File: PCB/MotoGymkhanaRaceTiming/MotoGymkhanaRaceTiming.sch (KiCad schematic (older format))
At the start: 27 parts, among them U1 LM2577T-ADJ_NOPB, U2 PC817, U3 PC817

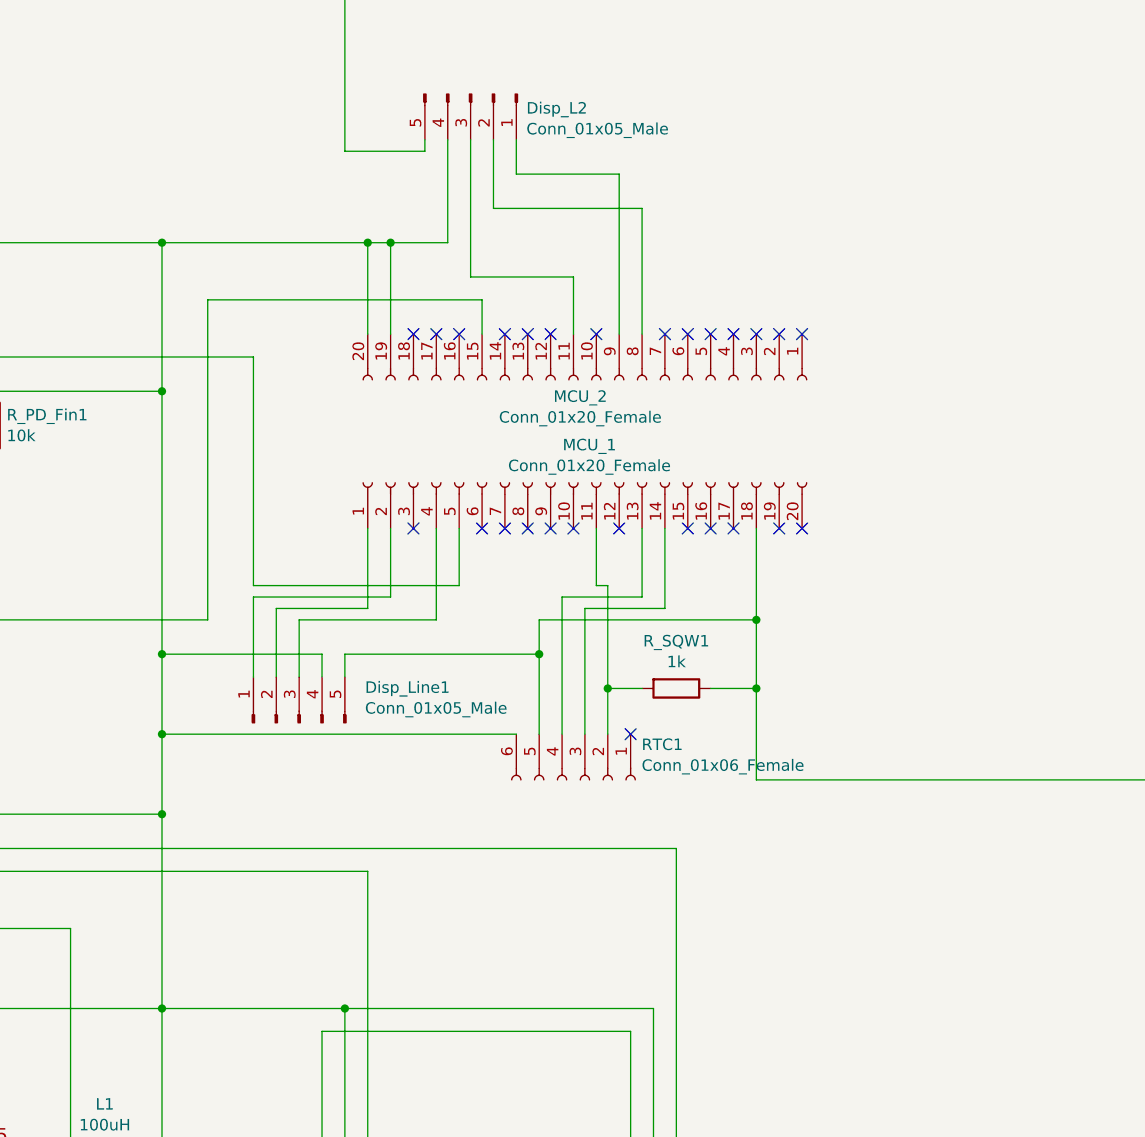
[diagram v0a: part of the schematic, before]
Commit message: Better PCB, now with jumpers (or headers to wire switches to) for configuration
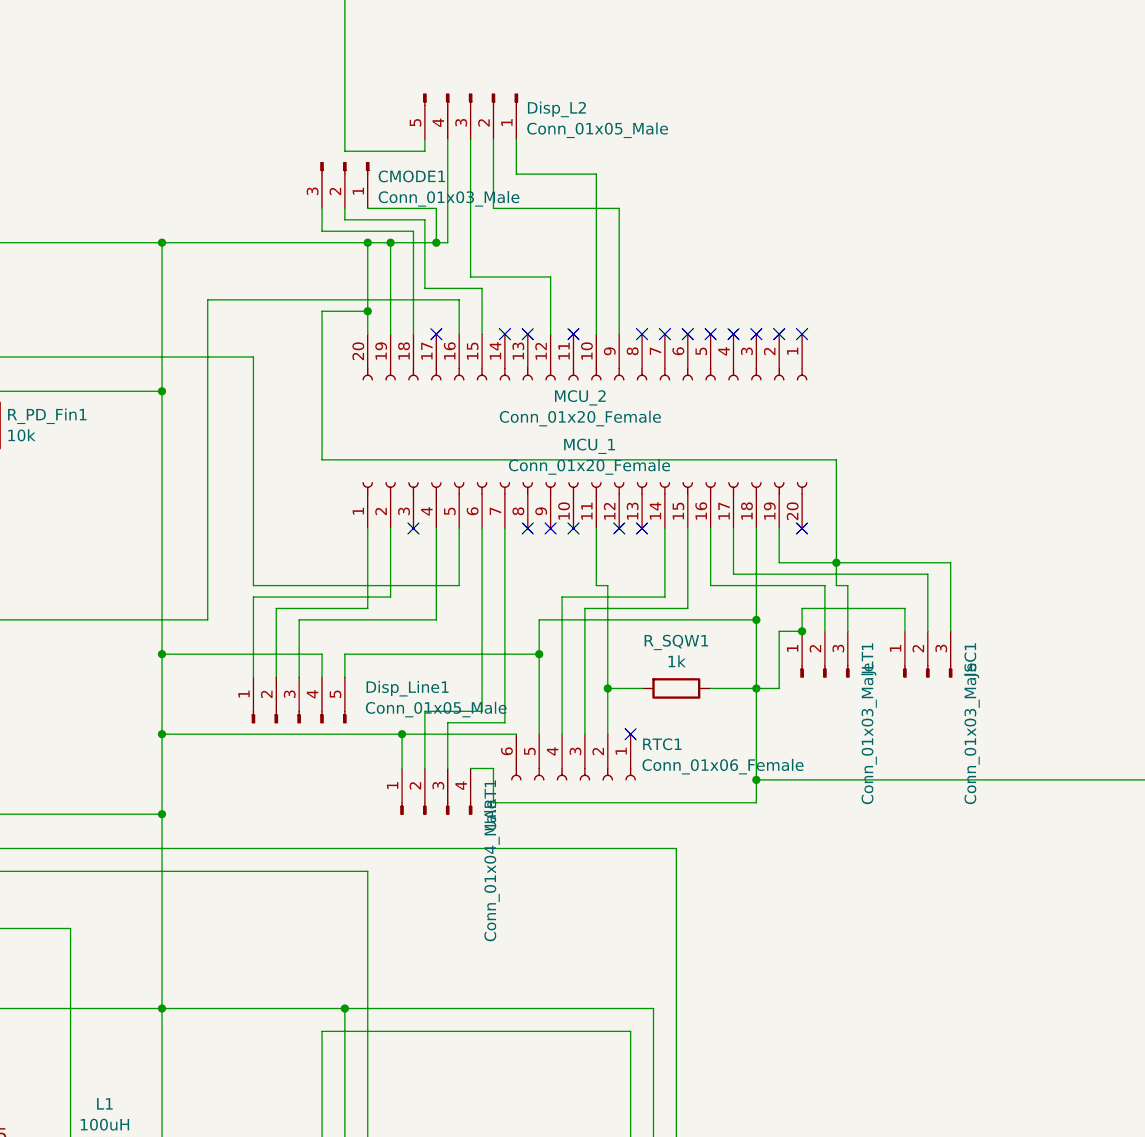
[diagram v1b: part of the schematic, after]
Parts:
- added CMODE1, JLT1, JSC1: Conn_01x03_Male, Connector_PinHeader_2.54mm:PinHeader_1x03_P2.54mm_Vertical, symbol Connector:Conn_01x03_Male
- added UART1: Conn_01x04_Male, Connector_PinHeader_2.54mm:PinHeader_1x04_P2.54mm_Vertical, symbol Connector:Conn_01x04_Male
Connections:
- net at MCU_2.10 (Pin_10): now also Disp_L2.1 (Pin_1)
- net at MCU_2.11 (Pin_11): no longer Disp_L2.3 (Pin_3)
- net at MCU_2.12 (Pin_12): now also Disp_L2.3 (Pin_3)
- net at LED_FIN1.2 (A), R_PD_Fin1.2, U3.3: now also MCU_2.16 (Pin_16); no longer MCU_2.15 (Pin_15)
- net at MCU_2.18 (Pin_18): now also CMODE1.3 (Pin_3)
- net at C1.2, C2.1, C3.2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: now also MCU_1.19 (Pin_19), CMODE1.1 (Pin_1), JLT1.3 (Pin_3), JSC1.3 (Pin_3), UART1.1 (Pin_1)
- net at MCU_2.8 (Pin_8): no longer Disp_L2.2 (Pin_2)
- net at MCU_2.9 (Pin_9): now also Disp_L2.2 (Pin_2); no longer Disp_L2.1 (Pin_1)
- net at MCU_1.13 (Pin_13): no longer RTC1.4 (Pin_4)
- net at MCU_1.14 (Pin_14): now also RTC1.4 (Pin_4); no longer RTC1.3 (Pin_3)
- net at MCU_1.15 (Pin_15): now also RTC1.3 (Pin_3)
- net at MCU_1.16 (Pin_16): now also JLT1.2 (Pin_2)
- net at MCU_1.17 (Pin_17): now also JSC1.2 (Pin_2)
- net at C1.1, C3.1, Disp_L2.5 (Pin_5)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: now also JLT1.1 (Pin_1), JSC1.1 (Pin_1), UART1.4 (Pin_4)
- net at MCU_1.6 (Pin_6): now also UART1.2 (Pin_2)
- net at MCU_1.7 (Pin_7): now also UART1.3 (Pin_3)
- new net: CMODE1.2 (Pin_2), MCU_2.15 (Pin_15)
- no-connect marks 30 -> 23
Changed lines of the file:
@@
 	1250 2750 3600 2750
 Wire Wire Line
-	4500 2750 4500 3150
+	4500 2750 4500 3050
 Wire Wire Line
 	4500 2750 4600 2750
@@
 Wire Wire Line
 	3800 4400 3800 3000
-Wire Wire Line
-	3800 3000 5000 3000
-Wire Wire Line
-	5000 3000 5000 3150
 Connection ~ 2850 4400
 Wire Wire Line
@@
 $EndComp
 Wire Wire Line
-	5150 4900 3600 4900
+	5150 4900 4650 4900
 Connection ~ 3600 4900
 Wire Wire Line
@@
 	5450 4900 5450 4350
 Wire Wire Line
-	5800 4350 5800 4000
-Wire Wire Line
-	5450 4350 5800 4350
-Wire Wire Line
 	5350 4900 5350 4300
-Wire Wire Line
-	5350 4300 5700 4300
-Wire Wire Line
-	5700 4300 5700 4000
 $Comp
 L Connector:Conn_01x05_Male Disp_L2
@@
 	4850 2300 4850 2750
 Wire Wire Line
-	4850 2750 4600 2750
+	4850 2750 4800 2750
 Connection ~ 4600 2750
 Wire Wire Line
 	4950 2300 4950 2900
 Wire Wire Line
-	4950 2900 5400 2900
-Wire Wire Line
-	5400 2900 5400 3150
-Wire Wire Line
-	5600 3150 5600 2450
-Wire Wire Line
-	5600 2450 5150 2450
-Wire Wire Line
 	5150 2450 5150 2300
 Wire Wire Line
 	5050 2300 5050 2600
-Wire Wire Line
-	5050 2600 5700 2600
-Wire Wire Line
-	5700 2600 5700 3150
 Wire Wire Line
 	4400 4650 4400 4550
@@
 NoConn ~ 5900 3150
 NoConn ~ 5800 3150
-NoConn ~ 5500 3150
-NoConn ~ 5300 3150
 NoConn ~ 5200 3150
 NoConn ~ 5100 3150
-NoConn ~ 4900 3150
 NoConn ~ 4800 3150
-NoConn ~ 4700 3150
 NoConn ~ 6400 4000
-NoConn ~ 6300 4000
-NoConn ~ 6100 4000
-NoConn ~ 6000 4000
-NoConn ~ 5900 4000
 NoConn ~ 5600 4000
 NoConn ~ 5400 4000
 NoConn ~ 5300 4000
 NoConn ~ 5200 4000
-NoConn ~ 5100 4000
-NoConn ~ 5000 4000
 NoConn ~ 4700 4000
 NoConn ~ 5650 4900
@@
 	1150 2050 1250 2050
 Connection ~ 1150 1950
+Wire Wire Line
+	5450 4350 5900 4350
+Wire Wire Line
+	5900 4350 5900 4000
+Wire Wire Line
+	5800 4300 5800 4000
+Wire Wire Line
+	5350 4300 5800 4300
+NoConn ~ 5700 4000
+Wire Wire Line
+	4500 3050 4300 3050
+Wire Wire Line
+	4300 3050 4300 3700
+Wire Wire Line
+	4300 3700 6550 3700
+Wire Wire Line
+	6550 3700 6550 4150
+Wire Wire Line
+	6550 4150 6300 4150
+Wire Wire Line
+	6300 4150 6300 4000
+Connection ~ 4500 3050
+Wire Wire Line
+	4500 3050 4500 3150
+$Comp
+L Connector:Conn_01x03_Male JLT1
+U 1 1 5ED22EE5
+P 6500 4650
+F 0 "JLT1" H 6654 4462 50  0000 R CNN
+F 1 "Conn_01x03_Male" H 6563 4462 50  0000 R CNN
+F 2 "Connector_PinHeader_2.54mm:PinHeader_1x03_P2.54mm_Vertical" H 6500 4650 50  0001 C CNN
+F 3 "~" H 6500 4650 50  0001 C CNN
+	1    6500 4650
+	0    -1   -1   0
+$EndComp
+$Comp
+L Connector:Conn_01x03_Male JSC1
+U 1 1 5ED24AEC
+P 6950 4650
+F 0 "JSC1" H 7104 4462 50  0000 R CNN
+F 1 "Conn_01x03_Male" H 7013 4462 50  0000 R CNN
+F 2 "Connector_PinHeader_2.54mm:PinHeader_1x03_P2.54mm_Vertical" H 6950 4650 50  0001 C CNN
+F 3 "~" H 6950 4650 50  0001 C CNN
+	1    6950 4650
+	0    -1   -1   0
+$EndComp
+Wire Wire Line
+	6500 4450 6500 4250
+Wire Wire Line
+	6500 4250 6000 4250
+Wire Wire Line
+	6000 4250 6000 4000
+Wire Wire Line
+	6950 4450 6950 4200
+Wire Wire Line
+	6950 4200 6100 4200
+Wire Wire Line
+	6100 4200 6100 4000
+Wire Wire Line
+	6200 4700 6300 4700
+Wire Wire Line
+	6300 4700 6300 4450
+Wire Wire Line
+	6300 4450 6400 4450
+Wire Wire Line
+	6400 4450 6400 4350
+Wire Wire Line
+	6400 4350 6850 4350
+Wire Wire Line
+	6850 4350 6850 4450
+Connection ~ 6400 4450
+Wire Wire Line
+	6550 4150 7050 4150
+Wire Wire Line
+	7050 4150 7050 4450
+Connection ~ 6550 4150
+Wire Wire Line
+	5050 2600 5600 2600
+Wire Wire Line
+	5600 2600 5600 3150
+Wire Wire Line
+	5150 2450 5500 2450
+Wire Wire Line
+	5500 2450 5500 3150
+NoConn ~ 5700 3150
+Wire Wire Line
+	6600 4450 6600 4250
+Wire Wire Line
+	6600 4250 6550 4250
+Wire Wire Line
+	6550 4250 6550 4150
+Wire Wire Line
+	4950 2900 5300 2900
+Wire Wire Line
+	5300 2900 5300 3150
+NoConn ~ 5400 3150
+$Comp
+L Connector:Conn_01x04_Male UART1
+U 1 1 5EDA4F4A
+P 4750 5250
+F 0 "UART1" H 4904 4962 50  0000 R CNN
+F 1 "Conn_01x04_Male" H 4813 4962 50  0000 R CNN
+F 2 "Connector_PinHeader_2.54mm:PinHeader_1x04_P2.54mm_Vertical" H 4750 5250 50  0001 C CNN
+F 3 "~" H 4750 5250 50  0001 C CNN
+	1    4750 5250
+	0    -1   -1   0
+$EndComp
+Wire Wire Line
+	5000 4000 5000 4800
+Wire Wire Line
+	4750 4800 4750 5050
+Wire Wire Line
+	5000 4800 4750 4800
+Wire Wire Line
+	4850 5050 4850 4850
+Wire Wire Line
+	4850 4850 5100 4850
+Wire Wire Line
+	5100 4850 5100 4000
+Wire Wire Line
+	4650 4900 4650 5050
+Connection ~ 4650 4900
+Wire Wire Line
+	4650 4900 3600 4900
+Wire Wire Line
+	4950 5050 5050 5050
+Wire Wire Line
+	5050 5050 5050 5200
+Wire Wire Line
+	5050 5200 6200 5200
+Wire Wire Line
+	6200 5200 6200 5100
+Connection ~ 6200 5100
+Wire Wire Line
+	3800 3000 4900 3000
+Wire Wire Line
+	4900 3000 4900 3150
+$Comp
+L Connector:Conn_01x03_Male CMODE1
+U 1 1 5EE0E5C1
+P 4400 2400
+F 0 "CMODE1" V 4462 2544 50  0000 L CNN
+F 1 "Conn_01x03_Male" V 4553 2544 50  0000 L CNN
+F 2 "Connector_PinHeader_2.54mm:PinHeader_1x03_P2.54mm_Vertical" H 4400 2400 50  0001 C CNN
+F 3 "~" H 4400 2400 50  0001 C CNN
+	1    4400 2400
+	0    1    1    0
+$EndComp
+Wire Wire Line
+	4300 2600 4300 2700
+Wire Wire Line
+	4300 2700 4700 2700
+Wire Wire Line
+	4400 2600 4400 2650
+Wire Wire Line
+	4400 2650 4750 2650
+Wire Wire Line
+	4750 2650 4750 2950
+Wire Wire Line
+	4750 2950 5000 2950
+Wire Wire Line
+	5000 2950 5000 3150
+Wire Wire Line
+	4500 2600 4800 2600
+Wire Wire Line
+	4800 2600 4800 2750
+Connection ~ 4800 2750
+Wire Wire Line
+	4600 2750 4800 2750
+Wire Wire Line
+	4700 2700 4700 3150
 $EndSCHEMATC

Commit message: PCB update
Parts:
- added Btn1, Btn2: Conn_01x02_Male, Connector_PinHeader_2.54mm:PinHeader_1x02_P2.54mm_Vertical, symbol Connector:Conn_01x02_Male
- added H1, H2, H3, H4: MountingHole_Pad, MountingHole:MountingHole_3.2mm_M3_Pad_Via, symbol Mechanical:MountingHole_Pad
- added R33: 33k, Resistor_THT:R_Axial_DIN0207_L6.3mm_D2.5mm_P10.16mm_Horizontal, symbol Device:R
- added R39: 3k9, Resistor_THT:R_Axial_DIN0207_L6.3mm_D2.5mm_P10.16mm_Horizontal, symbol Device:R
- added R_PD_B1, R_PD_B2: 10k, Resistor_THT:R_Axial_DIN0207_L6.3mm_D2.5mm_P10.16mm_Horizontal, symbol Device:R
- C1: footprint Capacitor_THT:CP_Radial_D13.0mm_P5.00mm -> Capacitor_THT:CP_Radial_D8.0mm_P5.00mm
- C2, C3: footprint Capacitor_THT:C_Radial_D10.0mm_H12.5mm_P5.00mm -> Capacitor_THT:C_Disc_D4.7mm_W2.5mm_P5.00mm
- C4: footprint Capacitor_THT:CP_Radial_D13.0mm_P5.00mm -> Capacitor_THT:CP_Radial_D10.0mm_P5.00mm
- Disp_L2, Disp_Line1: footprint Connector_PinHeader_2.54mm:PinHeader_1x05_P2.54mm_Horizontal -> MotoGymkhanaRaceTiming:DisplayLineConnector
- L1: footprint Inductor_THT:L_Toroid_Vertical_L10.0mm_W5.0mm_P5.08mm -> Inductor_THT:L_Radial_D7.0mm_P3.00mm
- SENS_FIN1, SENS_START1: footprint TerminalBlock:TerminalBlock_Altech_AK300-3_P5.00mm -> MotoGymkhanaRaceTiming:SensorConnector
- U1: symbol 2020-05-24_13-28-23:LM2577T-ADJ_NOPB -> MotoGymkhanaRaceTiming-rescue:LM2577T-ADJ_NOPB-2020-05-24_13-28-23
- UART1: footprint Connector_PinHeader_2.54mm:PinHeader_1x04_P2.54mm_Vertical -> MotoGymkhanaRaceTiming:UART
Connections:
- net at CMODE1.3 (Pin_3), MCU_2.18 (Pin_18): now also Btn1.1 (Pin_1), Btn2.1 (Pin_1)
- net at C1.2, C2.1, C3.2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: now also H1.1, H2.1, H3.1, H4.1, R39.1, R_PD_B1.2, R_PD_B2.2
- net at MCU_2.5 (Pin_5): now also Btn2.2 (Pin_2), R_PD_B2.1
- net at MCU_2.6 (Pin_6): now also Btn1.2 (Pin_2), R_PD_B1.1
- net at MCU_1.14 (Pin_14): now also RTC1.3 (Pin_3); no longer RTC1.4 (Pin_4)
- net at MCU_1.15 (Pin_15): now also RTC1.4 (Pin_4); no longer RTC1.3 (Pin_3)
- net at C4.1, D1.1 (K), SENS_FIN1.3 (Pin_3)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: now also R33.2; no longer U1.2 (FB)
- new net: R33.1, R39.2, U1.2 (FB)
- no-connect marks 23 -> 21

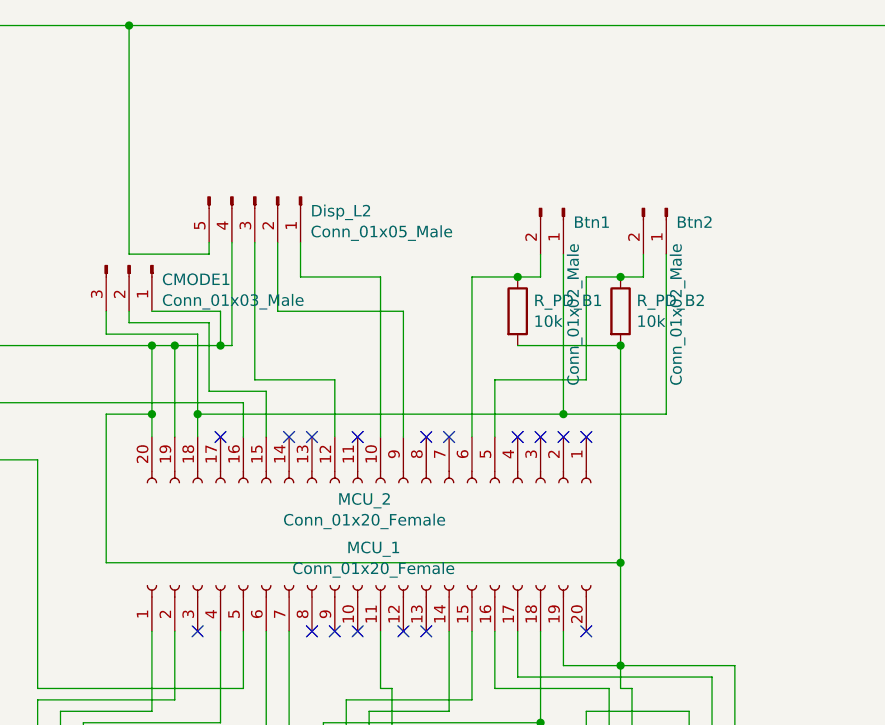
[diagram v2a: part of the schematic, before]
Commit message: Update for issue #9
- Adding text to RTC socket
- Adding UART2
- Trace width for 5V net updated
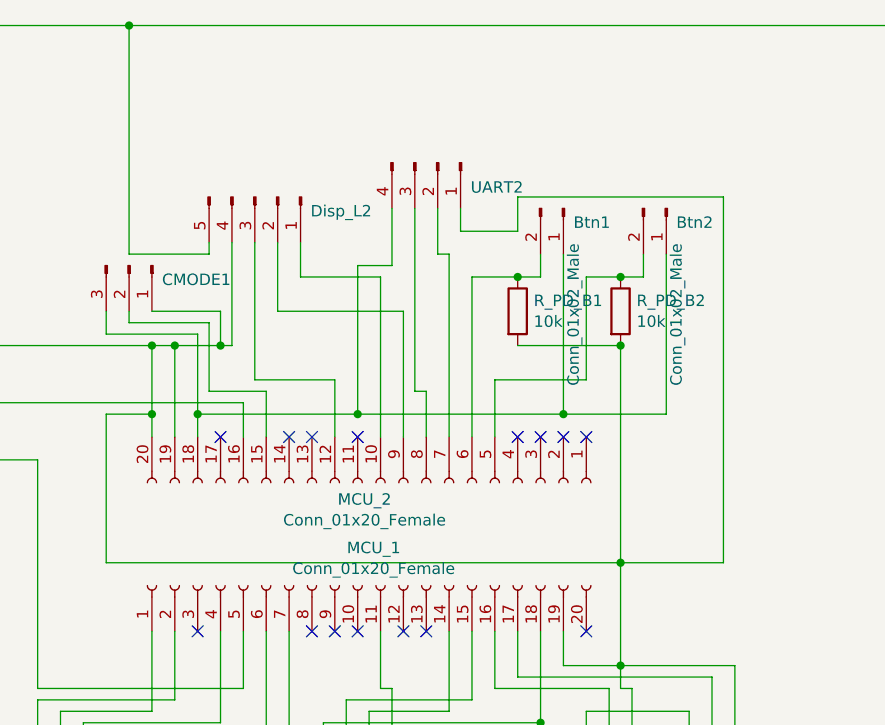
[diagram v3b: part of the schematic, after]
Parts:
- added UART2: Conn_01x04_Male, MotoGymkhanaRaceTiming:UART, symbol Connector:Conn_01x04_Male
- RTC1: footprint Connector_PinSocket_2.54mm:PinSocket_1x06_P2.54mm_Vertical -> MotoGymkhanaRaceTiming:RTC_Socket
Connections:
- net at Btn1.1 (Pin_1), Btn2.1 (Pin_1), CMODE1.3 (Pin_3)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: now also UART2.4 (Pin_4)
- net at C1.2, C2.1, C3.2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: now also UART2.1 (Pin_1)
- net at MCU_2.7 (Pin_7): now also UART2.2 (Pin_2)
- net at MCU_2.8 (Pin_8): now also UART2.3 (Pin_3)
- no-connect marks 21 -> 19
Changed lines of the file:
@@
 F 0 "RTC1" V 5296 5348 50  0000 L CNN
 F 1 "Conn_01x06_Female" V 5387 5348 50  0001 L CNN
-F 2 "Connector_PinSocket_2.54mm:PinSocket_1x06_P2.54mm_Vertical" H 5450 5100 50  0001 C CNN
+F 2 "MotoGymkhanaRaceTiming:RTC_Socket" H 5450 5100 50  0001 C CNN
 F 3 "~" H 5450 5100 50  0001 C CNN
 	1    5450 5100
@@
 P 4950 2100
 F 0 "Disp_L2" V 5012 2344 50  0000 L CNN
-F 1 "Conn_01x05_Male" V 5103 2344 50  0000 L CNN
+F 1 "Conn_01x05_Male" V 5103 2344 50  0001 L CNN
 F 2 "MotoGymkhanaRaceTiming:DisplayLineConnector" H 4950 2100 50  0001 C CNN
 F 3 "~" H 4950 2100 50  0001 C CNN
@@
 NoConn ~ 6200 3150
 NoConn ~ 6100 3150
-NoConn ~ 5800 3150
 NoConn ~ 5200 3150
 NoConn ~ 5100 3150
@@
 Wire Wire Line
 	5500 2450 5500 3150
-NoConn ~ 5700 3150
 Wire Wire Line
 	6600 4450 6600 4250
@@
 P 4400 2400
 F 0 "CMODE1" V 4462 2544 50  0000 L CNN
-F 1 "Conn_01x03_Male" V 4553 2544 50  0000 L CNN
+F 1 "Conn_01x03_Male" V 4553 2544 50  0001 L CNN
 F 2 "Connector_PinHeader_2.54mm:PinHeader_1x03_P2.54mm_Vertical" H 4400 2400 50  0001 C CNN
 F 3 "~" H 4400 2400 50  0001 C CNN
@@
 Connection ~ 6550 2450
 Wire Wire Line
-	4700 3050 6300 3050
+	4700 3050 5400 3050
 Wire Wire Line
 	6300 3050 6300 2350
@@
 Wire Wire Line
 	5800 4350 5800 4000
+Wire Wire Line
+	5550 2150 5550 2400
+Wire Wire Line
+	5550 2400 5400 2400
+Wire Wire Line
+	5400 2400 5400 3050
+Connection ~ 5400 3050
+Wire Wire Line
+	5400 3050 6300 3050
+$Comp
+L Connector:Conn_01x04_Male UART2
+U 1 1 5EE5EE8E
+P 5750 1950
+F 0 "UART2" V 5858 2094 50  0000 L CNN
+F 1 "Conn_01x04_Male" V 5903 2094 50  0001 L CNN
+F 2 "MotoGymkhanaRaceTiming:UART" H 5750 1950 50  0001 C CNN
+F 3 "~" H 5750 1950 50  0001 C CNN
+	1    5750 1950
+	0    1    1    0
+$EndComp
+Wire Wire Line
+	5850 2150 5850 2250
+Wire Wire Line
+	5850 2250 6100 2250
+Wire Wire Line
+	6100 2250 6100 2100
+Wire Wire Line
+	6100 2100 7000 2100
+Wire Wire Line
+	7000 2100 7000 3700
+Wire Wire Line
+	7000 3700 6550 3700
+Wire Wire Line
+	5750 2150 5750 2350
+Wire Wire Line
+	5750 2350 5800 2350
+Wire Wire Line
+	5800 2350 5800 3150
+Wire Wire Line
+	5650 2150 5650 2950
+Wire Wire Line
+	5650 2950 5700 2950
+Wire Wire Line
+	5700 2950 5700 3150
 $EndSCHEMATC

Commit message: Schematic optimizations
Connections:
- net GND: now reaches C1.2, C2.1, C3.2, C4.2, CMODE1.1 (Pin_1), Disp_L2.4 (Pin_4), Disp_Line1.4 (Pin_4), H1.1, H2.1, H3.1, H4.1, JLT1.3 (Pin_3), JSC1.3 (Pin_3), MCU_1.19 (Pin_19), MCU_2.19 (Pin_19), MCU_2.20 (Pin_20), PWR1.5 (GND), PWR1.6 (Shield), R1.1, R2.1, R39.1, RTC1.6 (Pin_6), R_PD_B1.2, R_PD_B2.2, R_PD_Fin1.1, R_PD_St1.1, SENS_FIN1.2 (Pin_2), SENS_START1.2 (Pin_2), U1.3 (GND), U2.2, U3.2, UART1.1 (Pin_1), UART2.1 (Pin_1)
- net +5V: now reaches C1.1, C3.1, Disp_L2.5 (Pin_5), Disp_Line1.5 (Pin_5), JLT1.1 (Pin_1), JSC1.1 (Pin_1), L1.2, MCU_1.18 (Pin_18), PWR1.1 (VBUS), RTC1.5 (Pin_5), R_SQW1.1, U1.5 (VIN), U2.4, U3.4, UART1.4 (Pin_4)
- net 12V: now reaches C4.1, D1.1 (K), R33.2, SENS_FIN1.3 (Pin_3), SENS_START1.3 (Pin_3)
